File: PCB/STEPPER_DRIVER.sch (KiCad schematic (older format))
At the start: 7 parts, among them J3 STEPPER, J4 STEPPER

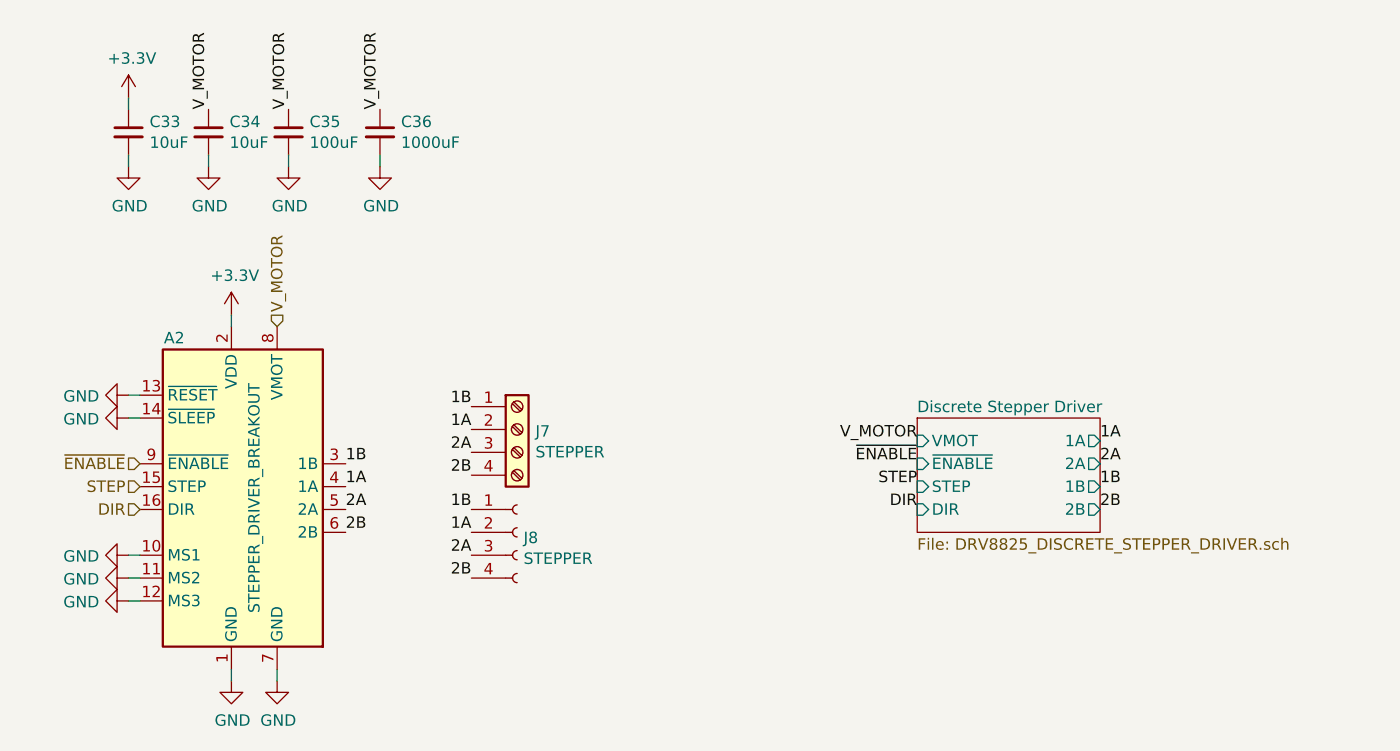
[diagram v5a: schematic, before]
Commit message: Increased VCC from 3v3 to 5v
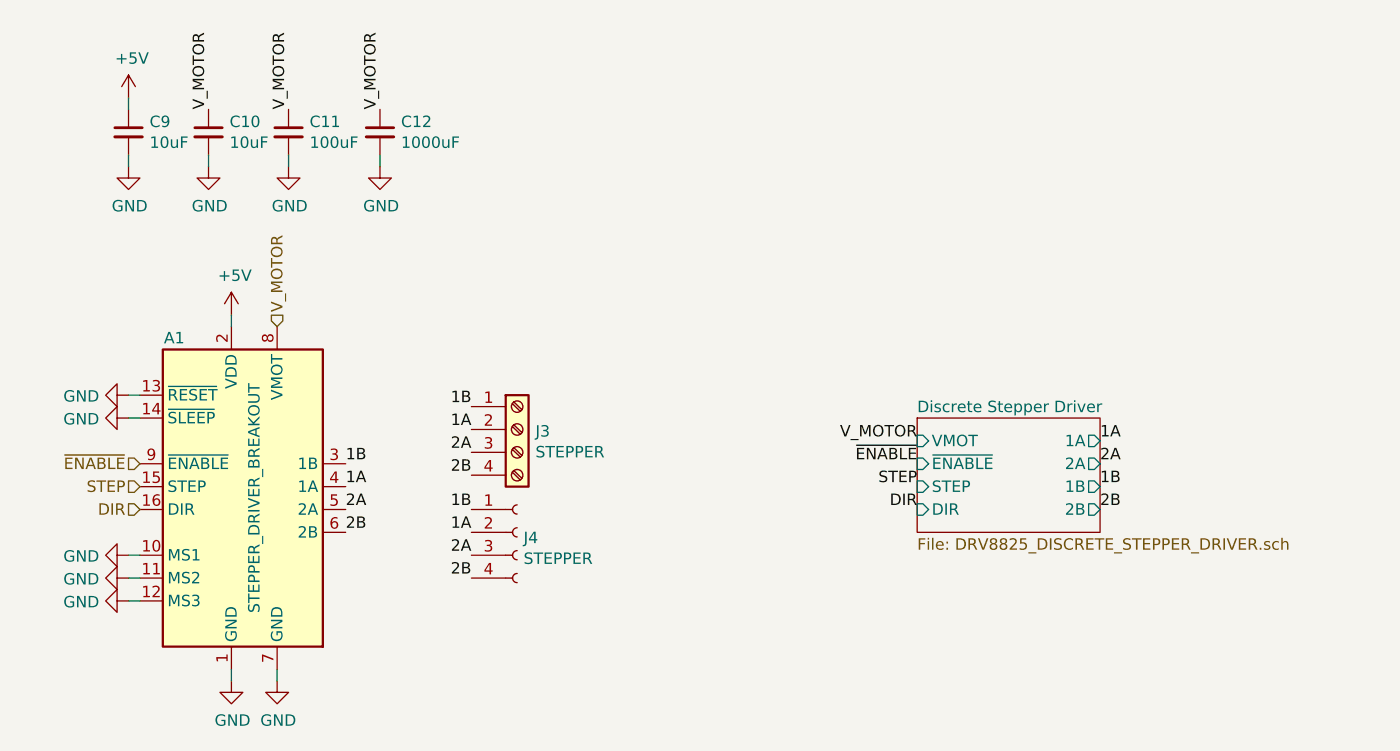
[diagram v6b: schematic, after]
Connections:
- net +3V3 renamed +5V
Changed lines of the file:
@@
 AR Path="/5E8A6686/5E8A6F90" Ref="A1"  Part="1"
 AR Path="/5E8813FF/5E8A6F90" Ref="A2"  Part="1"
-F 0 "A2" H 5450 4700 50  0000 C CNN
+F 0 "A1" H 5450 4700 50  0000 C CNN
 F 1 "STEPPER_DRIVER_BREAKOUT" V 5800 4000 50  0000 C CNN
 F 2 "Module:Pololu_Breakout-16_15.2x20.3mm" H 5975 3300 50  0001 L CNN
@@
 AR Path="/5E8A6686/5E8A7820" Ref="J4"  Part="1"
 AR Path="/5E8813FF/5E8A7820" Ref="J8"  Part="1"
-F 0 "J8" H 6978 4226 50  0000 L CNN
+F 0 "J4" H 6978 4226 50  0000 L CNN
 F 1 "STEPPER" H 6978 4135 50  0000 L CNN
 F 2 "" H 6950 4250 50  0001 C CNN
@@
 AR Path="/5E8A6686/5E8A82D9" Ref="J3"  Part="1"
 AR Path="/5E8813FF/5E8A82D9" Ref="J7"  Part="1"
-F 0 "J7" H 7030 3792 50  0000 L CNN
+F 0 "J3" H 7030 3792 50  0000 L CNN
 F 1 "STEPPER" H 7030 3701 50  0000 L CNN
 F 2 "" H 6950 3800 50  0001 C CNN
@@
 Text Label 6750 4000 2    50   ~ 0
 2B
-$Comp
-L power:+3.3V #PWR033
-U 1 1 5E8421AB
-P 5700 3300
-AR Path="/5E8A6686/5E8421AB" Ref="#PWR033"  Part="1"
-AR Path="/5E8813FF/5E8421AB" Ref="#PWR096"  Part="1"
-F 0 "#PWR096" H 5700 3150 50  0001 C CNN
-F 1 "+3.3V" H 5715 3473 50  0000 C CNN
-F 2 "" H 5700 3300 50  0001 C CNN
-F 3 "" H 5700 3300 50  0001 C CNN
-	1    5700 3300
-	1    0    0    -1
-$EndComp
 Wire Wire Line
 	5700 3300 5700 3350
@@
 AR Path="/5E8A6686/5E842853" Ref="#PWR034"  Part="1"
 AR Path="/5E8813FF/5E842853" Ref="#PWR097"  Part="1"
-F 0 "#PWR097" H 5700 4650 50  0001 C CNN
+F 0 "#PWR034" H 5700 4650 50  0001 C CNN
 F 1 "GND" H 5705 4727 50  0000 C CNN
 F 2 "" H 5700 4900 50  0001 C CNN
@@
 AR Path="/5E8A6686/5E842AD6" Ref="#PWR035"  Part="1"
 AR Path="/5E8813FF/5E842AD6" Ref="#PWR098"  Part="1"
-F 0 "#PWR098" H 5900 4650 50  0001 C CNN
+F 0 "#PWR035" H 5900 4650 50  0001 C CNN
 F 1 "GND" H 5905 4727 50  0000 C CNN
 F 2 "" H 5900 4900 50  0001 C CNN
@@
 AR Path="/5E8A6686/5E84D212" Ref="#PWR027"  Part="1"
 AR Path="/5E8813FF/5E84D212" Ref="#PWR090"  Part="1"
-F 0 "#PWR090" H 5250 3400 50  0001 C CNN
+F 0 "#PWR027" H 5250 3400 50  0001 C CNN
 F 1 "GND" V 5255 3522 50  0000 R CNN
 F 2 "" H 5250 3650 50  0001 C CNN
@@
 AR Path="/5E8A6686/5E8548E0" Ref="C11"  Part="1"
 AR Path="/5E8813FF/5E8548E0" Ref="C35"  Part="1"
-F 0 "C35" H 6042 2546 50  0000 L CNN
+F 0 "C11" H 6042 2546 50  0000 L CNN
 F 1 "100uF" H 6042 2455 50  0000 L CNN
 F 2 "" H 5950 2500 50  0001 C CNN
@@
 AR Path="/5E8A6686/5E8548E7" Ref="#PWR036"  Part="1"
 AR Path="/5E8813FF/5E8548E7" Ref="#PWR099"  Part="1"
-F 0 "#PWR099" H 5950 2400 50  0001 C CNN
+F 0 "#PWR036" H 5950 2400 50  0001 C CNN
 F 1 "GND" H 5955 2477 50  0000 C CNN
 F 2 "" H 5950 2650 50  0001 C CNN
@@
 AR Path="/5E8A6686/5E8572F7" Ref="C10"  Part="1"
 AR Path="/5E8813FF/5E8572F7" Ref="C34"  Part="1"
-F 0 "C34" H 5692 2546 50  0000 L CNN
+F 0 "C10" H 5692 2546 50  0000 L CNN
 F 1 "10uF" H 5692 2455 50  0000 L CNN
 F 2 "" H 5600 2500 50  0001 C CNN
@@
 AR Path="/5E8A6686/5E8572FE" Ref="#PWR032"  Part="1"
 AR Path="/5E8813FF/5E8572FE" Ref="#PWR095"  Part="1"
-F 0 "#PWR095" H 5600 2400 50  0001 C CNN
+F 0 "#PWR032" H 5600 2400 50  0001 C CNN
 F 1 "GND" H 5605 2477 50  0000 C CNN
 F 2 "" H 5600 2650 50  0001 C CNN
@@
 AR Path="/5E8A6686/5E857755" Ref="C12"  Part="1"
 AR Path="/5E8813FF/5E857755" Ref="C36"  Part="1"
-F 0 "C36" H 6442 2546 50  0000 L CNN
+F 0 "C12" H 6442 2546 50  0000 L CNN
 F 1 "1000uF" H 6442 2455 50  0000 L CNN
 F 2 "" H 6350 2500 50  0001 C CNN
@@
 AR Path="/5E8A6686/5E85775C" Ref="#PWR037"  Part="1"
 AR Path="/5E8813FF/5E85775C" Ref="#PWR0100"  Part="1"
-F 0 "#PWR0100" H 6350 2400 50  0001 C CNN
+F 0 "#PWR037" H 6350 2400 50  0001 C CNN
 F 1 "GND" H 6355 2477 50  0000 C CNN
 F 2 "" H 6350 2650 50  0001 C CNN
@@
 AR Path="/5E8A6686/5E860421" Ref="C9"  Part="1"
 AR Path="/5E8813FF/5E860421" Ref="C33"  Part="1"
-F 0 "C33" H 5342 2546 50  0000 L CNN
+F 0 "C9" H 5342 2546 50  0000 L CNN
 F 1 "10uF" H 5342 2455 50  0000 L CNN
 F 2 "" H 5250 2500 50  0001 C CNN
@@
 AR Path="/5E8A6686/5E860428" Ref="#PWR026"  Part="1"
 AR Path="/5E8813FF/5E860428" Ref="#PWR089"  Part="1"
-F 0 "#PWR089" H 5250 2400 50  0001 C CNN
+F 0 "#PWR026" H 5250 2400 50  0001 C CNN
 F 1 "GND" H 5255 2477 50  0000 C CNN
 F 2 "" H 5250 2650 50  0001 C CNN
@@
 Wire Wire Line
 	5250 2650 5250 2600
-$Comp
-L power:+3.3V #PWR025
-U 1 1 5E8608E5
-P 5250 2350
-AR Path="/5E8A6686/5E8608E5" Ref="#PWR025"  Part="1"
-AR Path="/5E8813FF/5E8608E5" Ref="#PWR088"  Part="1"
-F 0 "#PWR088" H 5250 2200 50  0001 C CNN
-F 1 "+3.3V" H 5265 2523 50  0000 C CNN
-F 2 "" H 5250 2350 50  0001 C CNN
-F 3 "" H 5250 2350 50  0001 C CNN
-	1    5250 2350
-	1    0    0    -1
-$EndComp
 Wire Wire Line
 	5250 2350 5250 2400
@@
 AR Path="/5E8A6686/5E8CF9B2" Ref="#PWR028"  Part="1"
 AR Path="/5E8813FF/5E8CF9B2" Ref="#PWR091"  Part="1"
-F 0 "#PWR091" H 5250 3500 50  0001 C CNN
+F 0 "#PWR028" H 5250 3500 50  0001 C CNN
 F 1 "GND" V 5255 3622 50  0000 R CNN
 F 2 "" H 5250 3750 50  0001 C CNN
@@
 AR Path="/5E8A6686/5E8FF25B" Ref="#PWR029"  Part="1"
 AR Path="/5E8813FF/5E8FF25B" Ref="#PWR092"  Part="1"
-F 0 "#PWR092" H 5250 4100 50  0001 C CNN
+F 0 "#PWR029" H 5250 4100 50  0001 C CNN
 F 1 "GND" V 5255 4222 50  0000 R CNN
 F 2 "" H 5250 4350 50  0001 C CNN
@@
 AR Path="/5E8A6686/5E8FF51C" Ref="#PWR030"  Part="1"
 AR Path="/5E8813FF/5E8FF51C" Ref="#PWR093"  Part="1"
-F 0 "#PWR093" H 5250 4200 50  0001 C CNN
+F 0 "#PWR030" H 5250 4200 50  0001 C CNN
 F 1 "GND" V 5255 4322 50  0000 R CNN
 F 2 "" H 5250 4450 50  0001 C CNN
@@
 AR Path="/5E8A6686/5E8FF61C" Ref="#PWR031"  Part="1"
 AR Path="/5E8813FF/5E8FF61C" Ref="#PWR094"  Part="1"
-F 0 "#PWR094" H 5250 4300 50  0001 C CNN
+F 0 "#PWR031" H 5250 4300 50  0001 C CNN
 F 1 "GND" V 5255 4422 50  0000 R CNN
 F 2 "" H 5250 4550 50  0001 C CNN
@@
 F9 "DIR" I L 8700 4150 50
 $EndSheet
+$Comp
+L power:+5V #PWR?
+U 1 1 5E90606A
+P 5250 2350
+F 0 "#PWR?" H 5250 2200 50  0001 C CNN
+F 1 "+5V" H 5265 2523 50  0000 C CNN
+F 2 "" H 5250 2350 50  0001 C CNN
+F 3 "" H 5250 2350 50  0001 C CNN
+	1    5250 2350
+	1    0    0    -1
+$EndComp
+$Comp
+L power:+5V #PWR?
+U 1 1 5E9062D0
+P 5700 3300
+F 0 "#PWR?" H 5700 3150 50  0001 C CNN
+F 1 "+5V" H 5715 3473 50  0000 C CNN
+F 2 "" H 5700 3300 50  0001 C CNN
+F 3 "" H 5700 3300 50  0001 C CNN
+	1    5700 3300
+	1    0    0    -1
+$EndComp
 $EndSCHEMATC

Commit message: Added Humidity and temperature sensors
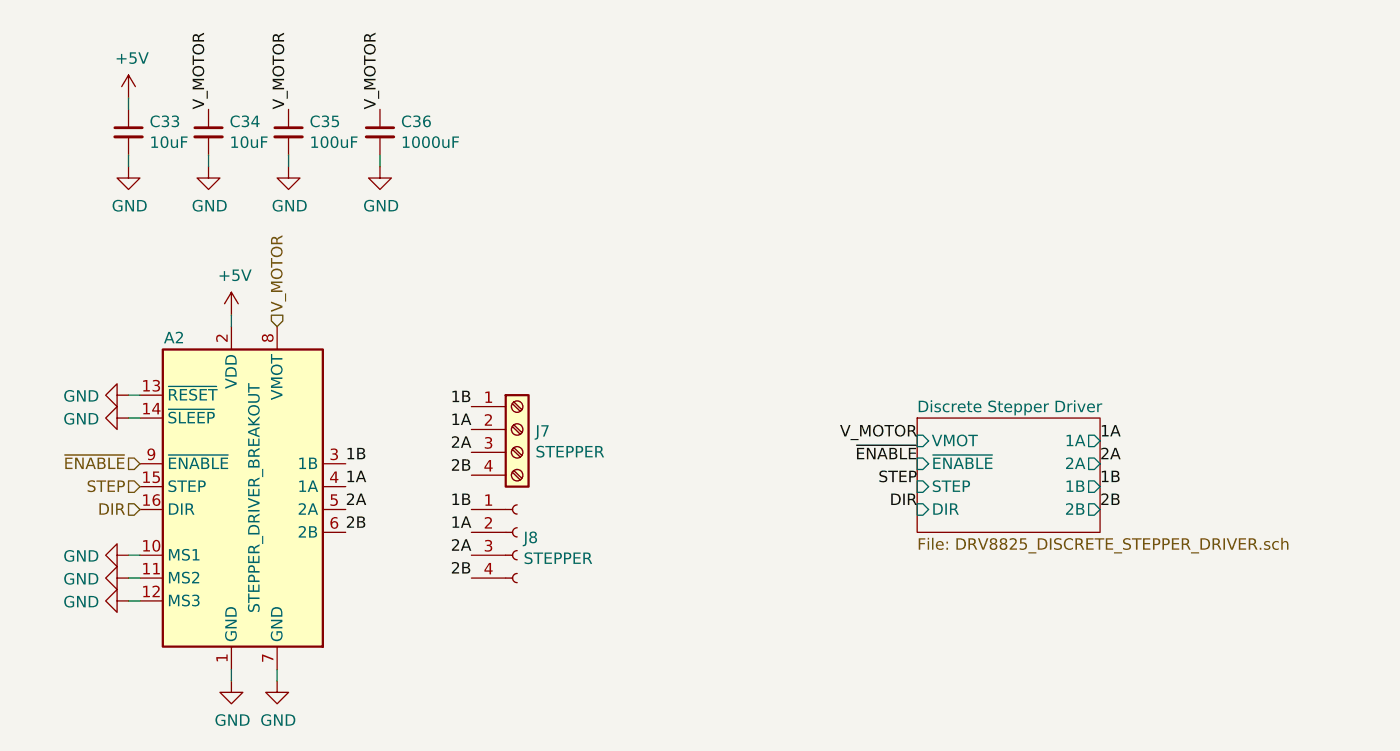
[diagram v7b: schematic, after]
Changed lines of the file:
@@
 AR Path="/5E8A6686/5E8A6F90" Ref="A1"  Part="1"
 AR Path="/5E8813FF/5E8A6F90" Ref="A2"  Part="1"
-F 0 "A1" H 5450 4700 50  0000 C CNN
+F 0 "A2" H 5450 4700 50  0000 C CNN
 F 1 "STEPPER_DRIVER_BREAKOUT" V 5800 4000 50  0000 C CNN
 F 2 "Module:Pololu_Breakout-16_15.2x20.3mm" H 5975 3300 50  0001 L CNN
@@
 AR Path="/5E8A6686/5E8A7820" Ref="J4"  Part="1"
 AR Path="/5E8813FF/5E8A7820" Ref="J8"  Part="1"
-F 0 "J4" H 6978 4226 50  0000 L CNN
+F 0 "J8" H 6978 4226 50  0000 L CNN
 F 1 "STEPPER" H 6978 4135 50  0000 L CNN
 F 2 "" H 6950 4250 50  0001 C CNN
@@
 AR Path="/5E8A6686/5E8A82D9" Ref="J3"  Part="1"
 AR Path="/5E8813FF/5E8A82D9" Ref="J7"  Part="1"
-F 0 "J3" H 7030 3792 50  0000 L CNN
+F 0 "J7" H 7030 3792 50  0000 L CNN
 F 1 "STEPPER" H 7030 3701 50  0000 L CNN
 F 2 "" H 6950 3800 50  0001 C CNN
@@
 P 5700 4900
 AR Path="/5E8A6686/5E842853" Ref="#PWR034"  Part="1"
-AR Path="/5E8813FF/5E842853" Ref="#PWR097"  Part="1"
-F 0 "#PWR034" H 5700 4650 50  0001 C CNN
+AR Path="/5E8813FF/5E842853" Ref="#PWR0100"  Part="1"
+F 0 "#PWR0100" H 5700 4650 50  0001 C CNN
 F 1 "GND" H 5705 4727 50  0000 C CNN
 F 2 "" H 5700 4900 50  0001 C CNN
@@
 P 5900 4900
 AR Path="/5E8A6686/5E842AD6" Ref="#PWR035"  Part="1"
-AR Path="/5E8813FF/5E842AD6" Ref="#PWR098"  Part="1"
-F 0 "#PWR035" H 5900 4650 50  0001 C CNN
+AR Path="/5E8813FF/5E842AD6" Ref="#PWR0101"  Part="1"
+F 0 "#PWR0101" H 5900 4650 50  0001 C CNN
 F 1 "GND" H 5905 4727 50  0000 C CNN
 F 2 "" H 5900 4900 50  0001 C CNN
@@
 P 5250 3650
 AR Path="/5E8A6686/5E84D212" Ref="#PWR027"  Part="1"
-AR Path="/5E8813FF/5E84D212" Ref="#PWR090"  Part="1"
-F 0 "#PWR027" H 5250 3400 50  0001 C CNN
+AR Path="/5E8813FF/5E84D212" Ref="#PWR093"  Part="1"
+F 0 "#PWR093" H 5250 3400 50  0001 C CNN
 F 1 "GND" V 5255 3522 50  0000 R CNN
 F 2 "" H 5250 3650 50  0001 C CNN
@@
 AR Path="/5E8A6686/5E8548E0" Ref="C11"  Part="1"
 AR Path="/5E8813FF/5E8548E0" Ref="C35"  Part="1"
-F 0 "C11" H 6042 2546 50  0000 L CNN
+F 0 "C35" H 6042 2546 50  0000 L CNN
 F 1 "100uF" H 6042 2455 50  0000 L CNN
 F 2 "" H 5950 2500 50  0001 C CNN
@@
 P 5950 2650
 AR Path="/5E8A6686/5E8548E7" Ref="#PWR036"  Part="1"
-AR Path="/5E8813FF/5E8548E7" Ref="#PWR099"  Part="1"
-F 0 "#PWR036" H 5950 2400 50  0001 C CNN
+AR Path="/5E8813FF/5E8548E7" Ref="#PWR0102"  Part="1"
+F 0 "#PWR0102" H 5950 2400 50  0001 C CNN
 F 1 "GND" H 5955 2477 50  0000 C CNN
 F 2 "" H 5950 2650 50  0001 C CNN
@@
 AR Path="/5E8A6686/5E8572F7" Ref="C10"  Part="1"
 AR Path="/5E8813FF/5E8572F7" Ref="C34"  Part="1"
-F 0 "C10" H 5692 2546 50  0000 L CNN
+F 0 "C34" H 5692 2546 50  0000 L CNN
 F 1 "10uF" H 5692 2455 50  0000 L CNN
 F 2 "" H 5600 2500 50  0001 C CNN
@@
 P 5600 2650
 AR Path="/5E8A6686/5E8572FE" Ref="#PWR032"  Part="1"
-AR Path="/5E8813FF/5E8572FE" Ref="#PWR095"  Part="1"
-F 0 "#PWR032" H 5600 2400 50  0001 C CNN
+AR Path="/5E8813FF/5E8572FE" Ref="#PWR098"  Part="1"
+F 0 "#PWR098" H 5600 2400 50  0001 C CNN
 F 1 "GND" H 5605 2477 50  0000 C CNN
 F 2 "" H 5600 2650 50  0001 C CNN
@@
 AR Path="/5E8A6686/5E857755" Ref="C12"  Part="1"
 AR Path="/5E8813FF/5E857755" Ref="C36"  Part="1"
-F 0 "C12" H 6442 2546 50  0000 L CNN
+F 0 "C36" H 6442 2546 50  0000 L CNN
 F 1 "1000uF" H 6442 2455 50  0000 L CNN
 F 2 "" H 6350 2500 50  0001 C CNN
@@
 P 6350 2650
 AR Path="/5E8A6686/5E85775C" Ref="#PWR037"  Part="1"
-AR Path="/5E8813FF/5E85775C" Ref="#PWR0100"  Part="1"
-F 0 "#PWR037" H 6350 2400 50  0001 C CNN
+AR Path="/5E8813FF/5E85775C" Ref="#PWR0103"  Part="1"
+F 0 "#PWR0103" H 6350 2400 50  0001 C CNN
 F 1 "GND" H 6355 2477 50  0000 C CNN
 F 2 "" H 6350 2650 50  0001 C CNN
@@
 AR Path="/5E8A6686/5E860421" Ref="C9"  Part="1"
 AR Path="/5E8813FF/5E860421" Ref="C33"  Part="1"
-F 0 "C9" H 5342 2546 50  0000 L CNN
+F 0 "C33" H 5342 2546 50  0000 L CNN
 F 1 "10uF" H 5342 2455 50  0000 L CNN
 F 2 "" H 5250 2500 50  0001 C CNN
@@
 P 5250 2650
 AR Path="/5E8A6686/5E860428" Ref="#PWR026"  Part="1"
-AR Path="/5E8813FF/5E860428" Ref="#PWR089"  Part="1"
-F 0 "#PWR026" H 5250 2400 50  0001 C CNN
+AR Path="/5E8813FF/5E860428" Ref="#PWR092"  Part="1"
+F 0 "#PWR092" H 5250 2400 50  0001 C CNN
 F 1 "GND" H 5255 2477 50  0000 C CNN
 F 2 "" H 5250 2650 50  0001 C CNN
@@
 P 5250 3750
 AR Path="/5E8A6686/5E8CF9B2" Ref="#PWR028"  Part="1"
-AR Path="/5E8813FF/5E8CF9B2" Ref="#PWR091"  Part="1"
-F 0 "#PWR028" H 5250 3500 50  0001 C CNN
+AR Path="/5E8813FF/5E8CF9B2" Ref="#PWR094"  Part="1"
+F 0 "#PWR094" H 5250 3500 50  0001 C CNN
 F 1 "GND" V 5255 3622 50  0000 R CNN
 F 2 "" H 5250 3750 50  0001 C CNN
@@
 P 5250 4350
 AR Path="/5E8A6686/5E8FF25B" Ref="#PWR029"  Part="1"
-AR Path="/5E8813FF/5E8FF25B" Ref="#PWR092"  Part="1"
-F 0 "#PWR029" H 5250 4100 50  0001 C CNN
+AR Path="/5E8813FF/5E8FF25B" Ref="#PWR095"  Part="1"
+F 0 "#PWR095" H 5250 4100 50  0001 C CNN
 F 1 "GND" V 5255 4222 50  0000 R CNN
 F 2 "" H 5250 4350 50  0001 C CNN
@@
 P 5250 4450
 AR Path="/5E8A6686/5E8FF51C" Ref="#PWR030"  Part="1"
-AR Path="/5E8813FF/5E8FF51C" Ref="#PWR093"  Part="1"
-F 0 "#PWR030" H 5250 4200 50  0001 C CNN
+AR Path="/5E8813FF/5E8FF51C" Ref="#PWR096"  Part="1"
+F 0 "#PWR096" H 5250 4200 50  0001 C CNN
 F 1 "GND" V 5255 4322 50  0000 R CNN
 F 2 "" H 5250 4450 50  0001 C CNN
@@
 P 5250 4550
 AR Path="/5E8A6686/5E8FF61C" Ref="#PWR031"  Part="1"
-AR Path="/5E8813FF/5E8FF61C" Ref="#PWR094"  Part="1"
-F 0 "#PWR031" H 5250 4300 50  0001 C CNN
+AR Path="/5E8813FF/5E8FF61C" Ref="#PWR097"  Part="1"
+F 0 "#PWR097" H 5250 4300 50  0001 C CNN
 F 1 "GND" V 5255 4422 50  0000 R CNN
 F 2 "" H 5250 4550 50  0001 C CNN
@@
 $EndSheet
 $Comp
-L power:+5V #PWR?
+L power:+5V #PWR025
 U 1 1 5E90606A
 P 5250 2350
-F 0 "#PWR?" H 5250 2200 50  0001 C CNN
+AR Path="/5E8A6686/5E90606A" Ref="#PWR025"  Part="1"
+AR Path="/5E8813FF/5E90606A" Ref="#PWR091"  Part="1"
+F 0 "#PWR091" H 5250 2200 50  0001 C CNN
 F 1 "+5V" H 5265 2523 50  0000 C CNN
 F 2 "" H 5250 2350 50  0001 C CNN
@@
 $EndComp
 $Comp
-L power:+5V #PWR?
+L power:+5V #PWR033
 U 1 1 5E9062D0
 P 5700 3300
-F 0 "#PWR?" H 5700 3150 50  0001 C CNN
+AR Path="/5E8A6686/5E9062D0" Ref="#PWR033"  Part="1"
+AR Path="/5E8813FF/5E9062D0" Ref="#PWR099"  Part="1"
+F 0 "#PWR099" H 5700 3150 50  0001 C CNN
 F 1 "+5V" H 5715 3473 50  0000 C CNN
 F 2 "" H 5700 3300 50  0001 C CNN
